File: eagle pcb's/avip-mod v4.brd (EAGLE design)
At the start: 63 x 21.1 mm, 36 parts, among them J4 0ohm, U1 14m2, U2 SN74LVC2G17DBV

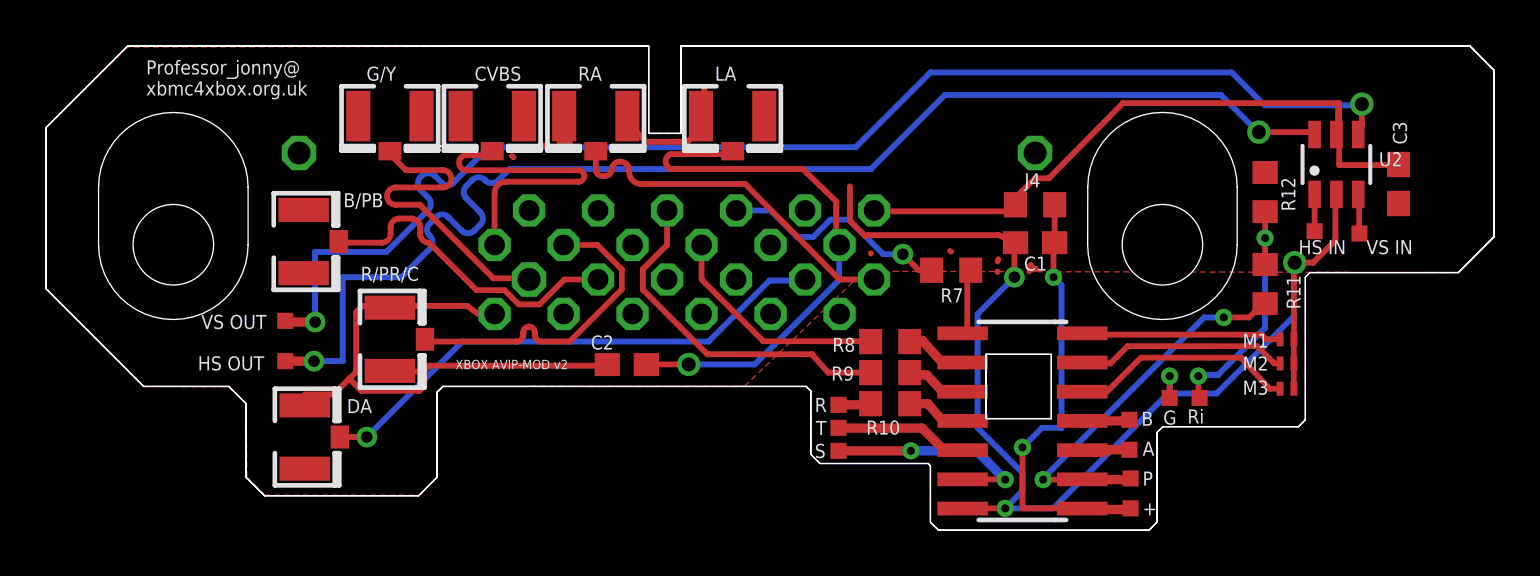
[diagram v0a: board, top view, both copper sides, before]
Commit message: Updates
Combined non stock items into single lib.
update pcb, clean up some more DRC issues.
reroute some traces to simplify design.
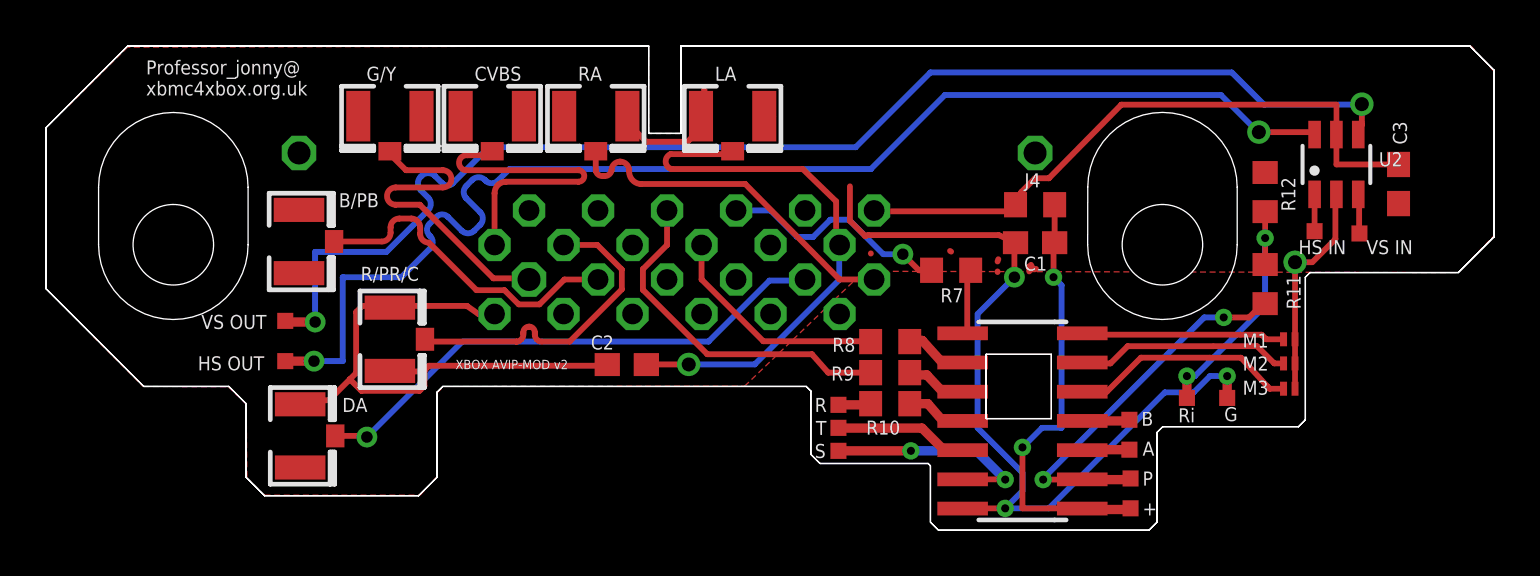
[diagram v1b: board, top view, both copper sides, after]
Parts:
- B/PB, CVBS, DA, G/Y, LA, R/PR/C, RA: device adafruit:U.FL -> XBOX:U.FL
- JP1, JP2, JP3: value JUMPER-SMT_2_NC_PASTE_NO-SILK -> JUMPER-SMT_NO-SILK; device SparkFun-Jumpers:SMT-JUMPER_2_NC_PASTE_NO-SILK -> XBOX:SMT-JUMPER
- U1: device picaxe-4:SO14 -> XBOX:SO14
- U2: device 74LV:SOT23-6 -> XBOX:SOT23-6
- moved GND 2.50 mm to (53.8, 5.70)
- moved RING 0.55 mm to (52.0, 5.70)
- moved DA 0.21 mm to (13.5, 4.05)
- moved B/PB 0.20 mm to (13.4, 12.5)
- moved JP1 0.10 mm to (56.5, 8.25)
- moved JP2 0.10 mm to (56.5, 7.20)
- moved JP3 0.10 mm to (56.5, 6.10)
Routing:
- net GND: track 91.7 -> 79.8 mm
- net VCC: track 29.2 -> 27.7 mm

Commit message: Fix PCB preview and update pictures
Conflict between mill and dimensions layer causing all PCB's to not show up in manufacture preview.
Add pictures of v3, v4 and v4 top PCB.
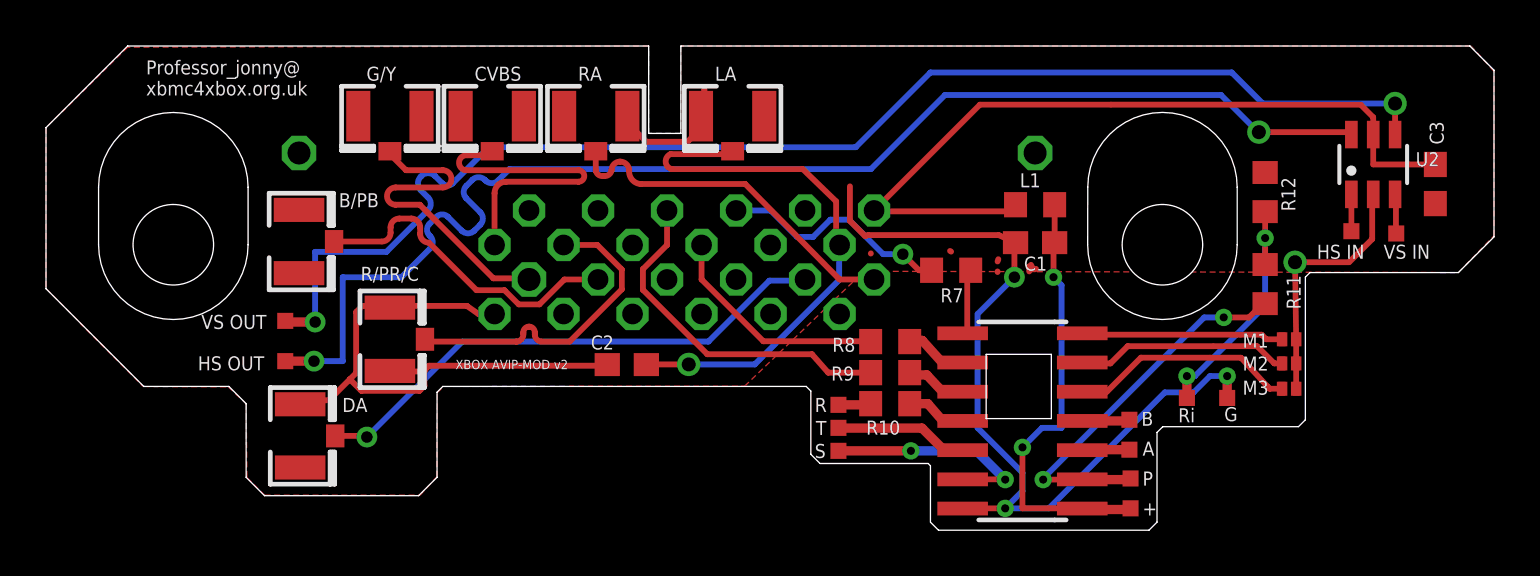
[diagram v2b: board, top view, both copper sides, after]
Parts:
- removed H_SYNC_IN, V_SYNC_IN: (no value), testpad:TP07SQ
- added HS_IN, VS_IN: (no value), testpad:TP07SQ
- moved C3 1.60 mm to (62.9, 15.0)
- moved U2 1.60 mm to (60.1, 15.8)
- turned JP1 to 0 degrees
- turned JP2 to 0 degrees
- turned JP3 to 0 degrees
- renumbered H_SYNC_OUT to HS_OUT, J4 to L1, PROG to P, RESET to R, RING to RI, SPEAK to S, TOGGLE to T, VCC2 to +, V_SYNC_OUT to VS_OUT
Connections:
- net H_SYNC_IN: now also HS_IN.TP; no longer H_SYNC_IN.TP
- net V_SYNC_IN: now also VS_IN.TP; no longer V_SYNC_IN.TP
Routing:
- net VCC: track 27.7 -> 34.9 mm
- net GND: track 79.8 -> 81.4 mm
- net H_SYNC_OUT: track 55.5 -> 57.1 mm
- net V_SYNC_OUT: track 56.6 -> 58.0 mm
